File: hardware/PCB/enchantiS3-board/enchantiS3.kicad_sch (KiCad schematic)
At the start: 74 parts, among them J1 USB_C_Receptacle_USB2.0, Q1 BSS138, Q2 BSS138, Q3 BSS138, SW1 B3U-1000P, SW2 B3U-1000P, U1 USBLC6-2P6, U2 MCP73871, U3 NCP167AMX330TBG, U4 NCP167AMX180TBG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

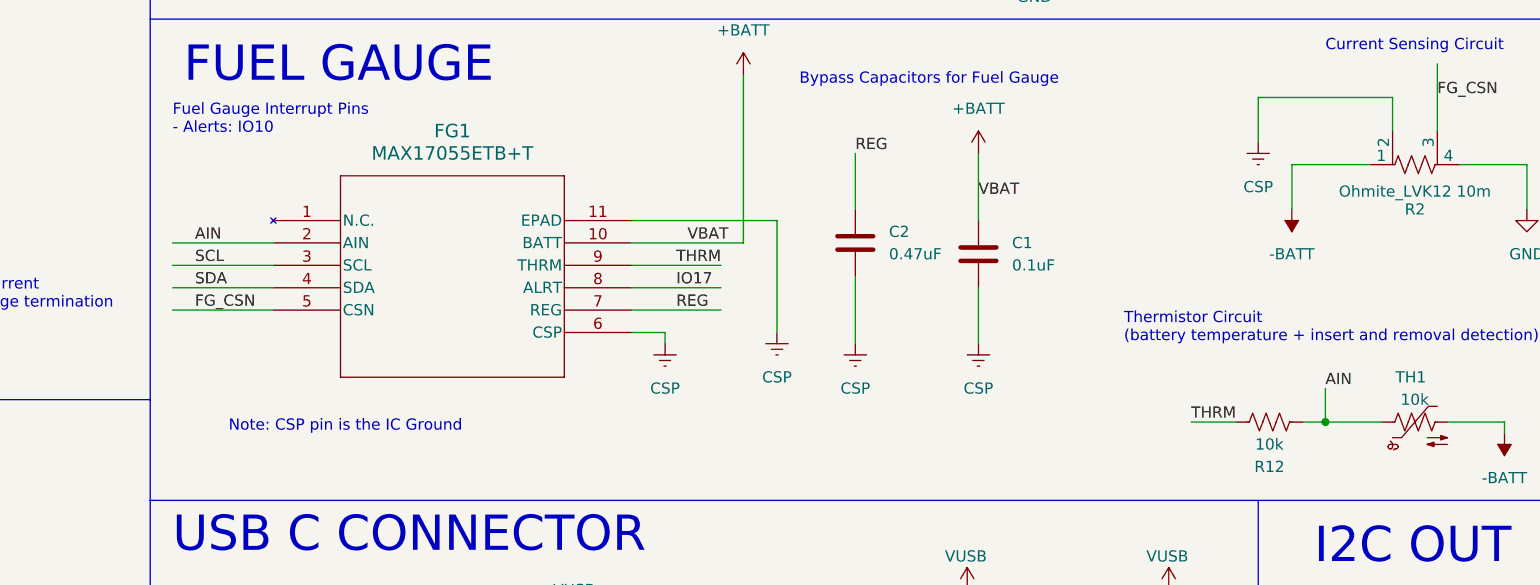
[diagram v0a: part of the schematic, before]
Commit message: update enchanti s3 pcb, cleaned up traces around fuel gauge
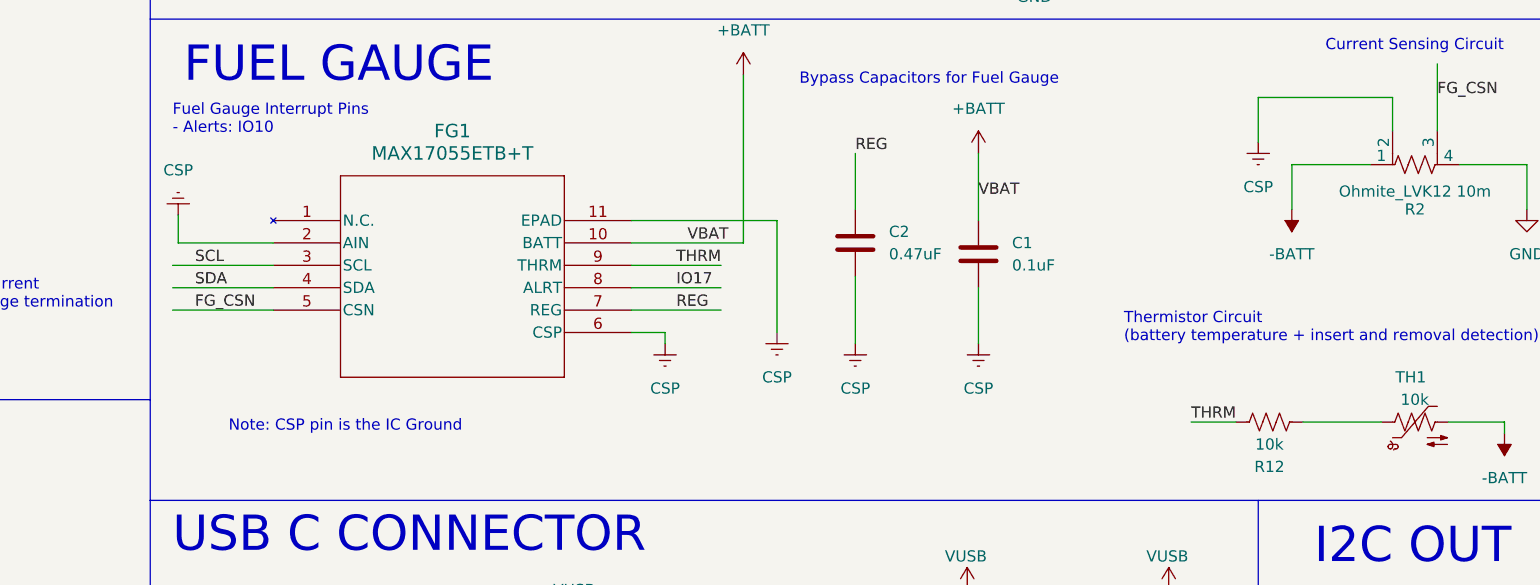
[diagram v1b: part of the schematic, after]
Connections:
- net CSP: now also FG1.2 (AIN)
- net AIN: no longer names the net of R12.1, TH1.1
- net AIN: no longer FG1.2 (AIN)
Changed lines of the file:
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@@
   (junction (at 309.88 33.02) (diameter 0) (color 0 0 0 0)
   )
-  (junction (at 243.84 166.37) (diameter 0) (color 0 0 0 0)
-  )
   (junction (at 363.22 45.72) (diameter 0) (color 0 0 0 0)
   )
@@
     (stroke (width 0) (type default))
   )
-  (wire (pts (xy 241.3 166.37) (xy 243.84 166.37))
-    (stroke (width 0) (type default))
-  )
   (wire (pts (xy 31.75 59.69) (xy 38.1 59.69))
     (stroke (width 0) (type default))
@@
     (stroke (width 0) (type default))
   )
-  (wire (pts (xy 243.84 162.56) (xy 243.84 166.37))
-    (stroke (width 0) (type default))
-  )
   (wire (pts (xy 382.27 96.52) (xy 391.16 96.52))
     (stroke (width 0) (type default))
@@
     (stroke (width 0) (type default))
   )
-  (wire (pts (xy 113.03 146.05) (xy 124.46 146.05))
-    (stroke (width 0) (type default))
-  )
   (polyline (pts (xy 408.94 110.49) (xy 408.94 111.76))
     (stroke (width 0) (type default))
@@
     (stroke (width 0) (type default))
   )
-  (wire (pts (xy 243.84 166.37) (xy 250.19 166.37))
+  (wire (pts (xy 241.3 166.37) (xy 250.19 166.37))
     (stroke (width 0) (type default))
   )
@@
     (stroke (width 0) (type default))
   )
+  (wire (pts (xy 113.665 142.875) (xy 113.665 146.05))
+    (stroke (width 0) (type default))
+  )
   (wire (pts (xy 30.48 44.45) (xy 38.1 44.45))
     (stroke (width 0) (type default))
@@
     (stroke (width 0) (type default))
   )
+  (wire (pts (xy 113.665 146.05) (xy 124.46 146.05))
+    (stroke (width 0) (type default))
+  )
   (wire (pts (xy 379.73 162.56) (xy 387.35 162.56))
     (stroke (width 0) (type default))
@@
     (effects (font (size 1.27 1.27)) (justify left bottom))
   )
-  (label "AIN" (at 115.57 146.05 0) (fields_autoplaced)
-    (effects (font (size 1.27 1.27)) (justify left bottom))
-  )
   (label "COPI" (at 214.63 256.54 180) (fields_autoplaced)
     (effects (font (size 1.27 1.27)) (justify right bottom))
@@
     (effects (font (size 1.27 1.27)) (justify left bottom))
   )
-  (label "AIN" (at 243.84 162.56 0) (fields_autoplaced)
-    (effects (font (size 1.27 1.27)) (justify left bottom))
-  )
   (label "VBAT" (at 171.45 146.05 0) (fields_autoplaced)
     (effects (font (size 1.27 1.27)) (justify left bottom))
@@
         )
       )
+    )
+  )
+  (symbol (lib_id "max17055-symbol:CSP") (at 113.665 141.605 180) (unit 1)
+    (in_bom yes) (on_board yes) (dnp no) (fields_autoplaced)
+    (property "Reference" "#ICGND05" (at 113.665 135.255 0)
+      (effects (font (size 1.27 1.27)) hide)
+    )
+    (property "Value" "CSP" (at 113.665 137.795 0)
+      (effects (font (size 1.27 1.27)))
+    )
+    (property "Footprint" "" (at 117.475 141.605 0)
+      (effects (font (size 1.27 1.27)) hide)
+    )
+    (property "Datasheet" "" (at 117.475 141.605 0)
+      (effects (font (size 1.27 1.27)) hide)
+    )
+    (pin "1")
+    (instances
+      (project "enchantiS3"
+        (path "/1e57a4ff-0c95-4e2b-9e56-d9bf8e99c9a1"
+          (reference "#ICGND05") (unit 1)
+        )
+      )
+      (project "tstick_pcb"
+        (path "/ecdbf224-0069-4dc3-a7df-492909ab59c7"
+          (reference "#ICGND04") (unit 1)
+        )
+      )

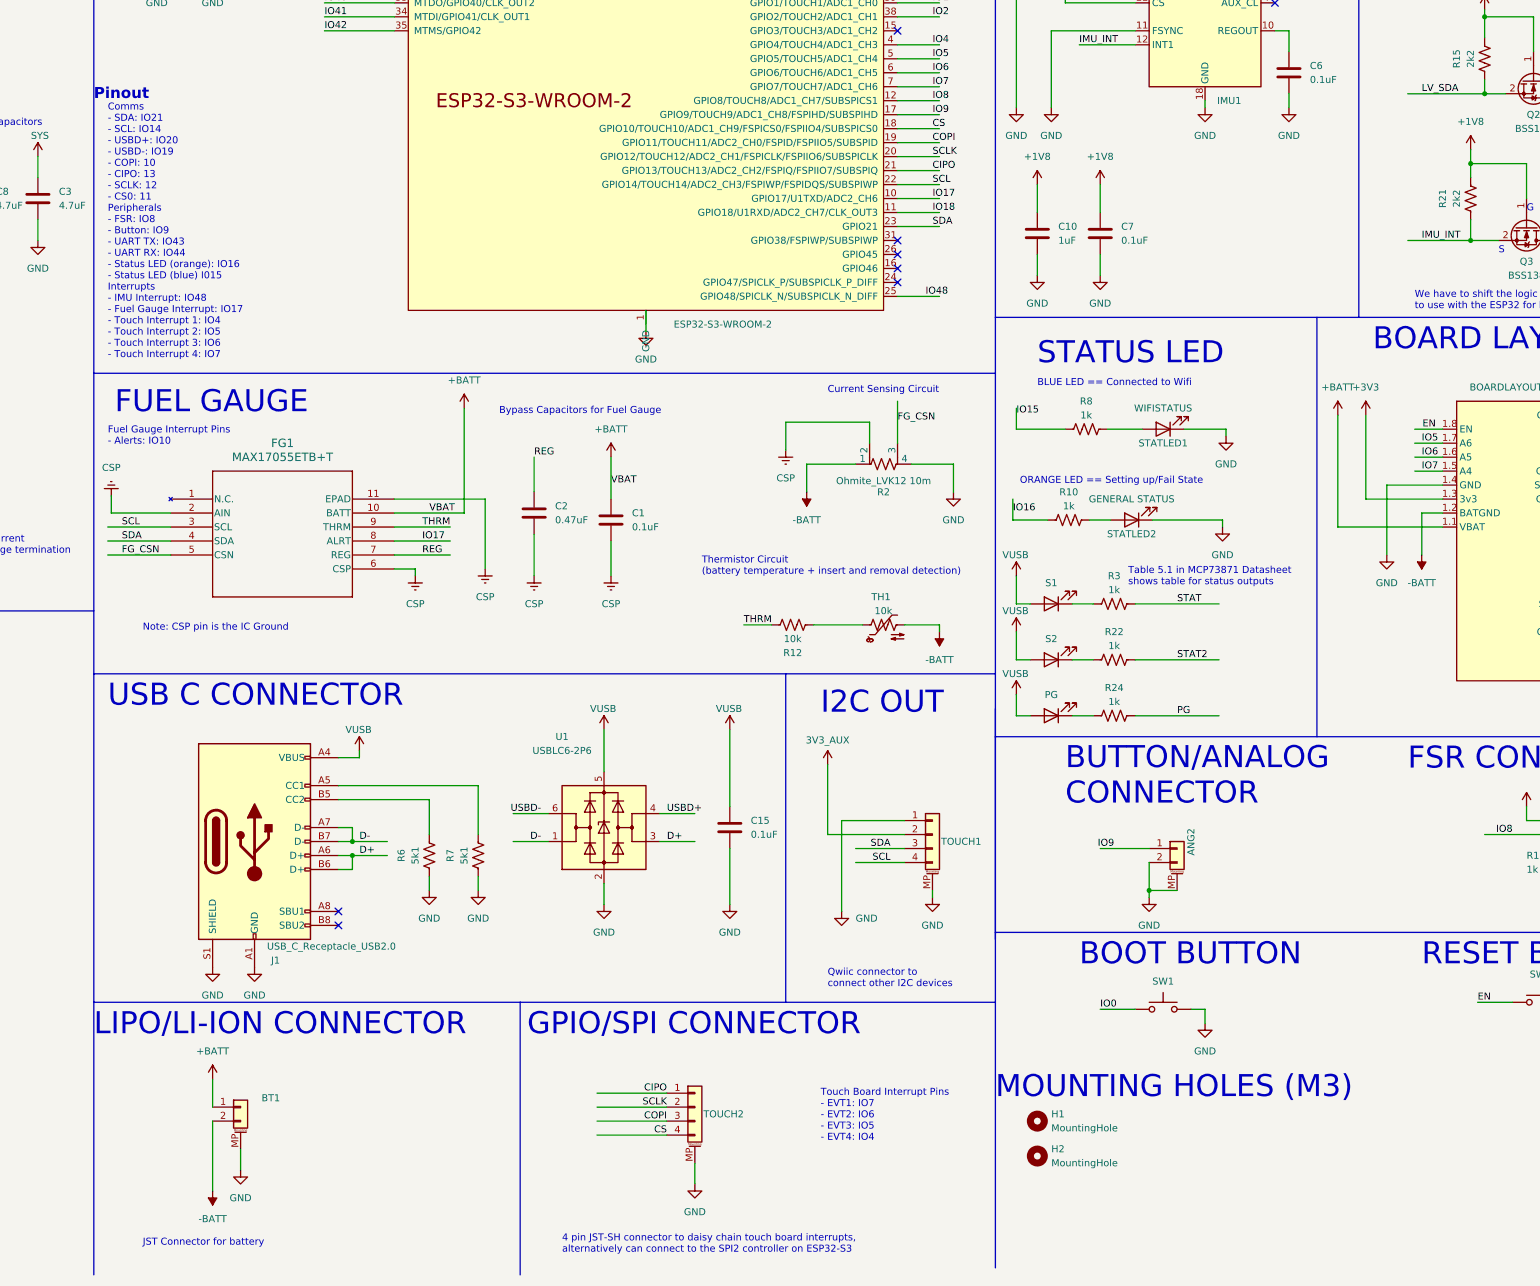
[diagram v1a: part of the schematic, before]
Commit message: changed to MAX17262 fuel gauge, removed unneeded part libraries
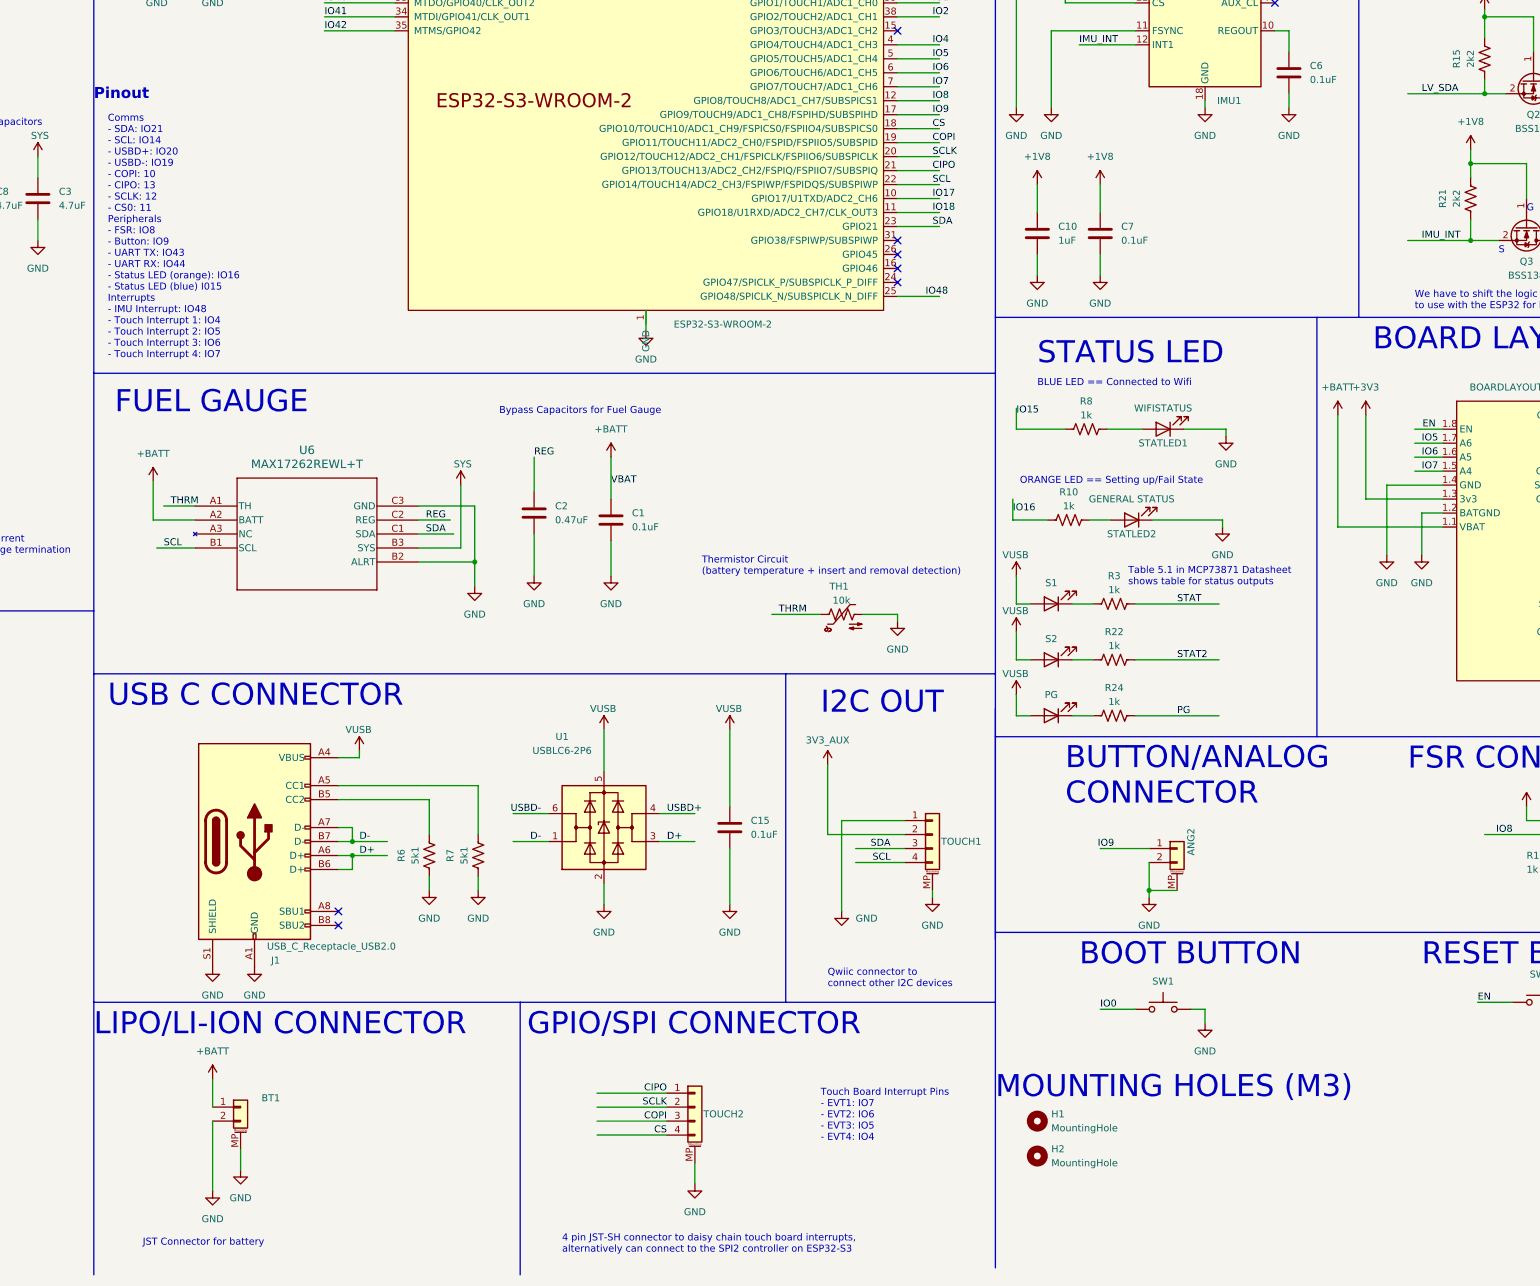
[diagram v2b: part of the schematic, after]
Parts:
- removed FG1: MAX17055ETB+T, max17055-footprints:21-100013A_T102A2&plus_1C_MXM, symbol max17055-symbol:MAX17055ETB+T
- removed R12: 10k, Resistor_SMD:R_0402_1005Metric, symbol Device:R_US
- removed R2: Ohmite_LVK12 10m, ul_LVK12R010CER-footprints:LVK12_OHM-L, symbol Device:R_Shunt_US
- added SYS7: SYS, symbol power-symbols:VSYS
- added U6: MAX17262REWL+T, max17262-footprints:21-100221A_W91G1&plus_3_MXM, symbol max17262:MAX17262REWL+T
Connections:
- net -BATT is gone; now on net GND: BOARDLAYOUT1.1.2 (BATGND), BT1.2 (Pin_2), TH1.2
- net CSP is gone; now on net GND: C1.2, C2.2
- net +BATT: now also U6.A2 (BATT)
- net GND: now also U6.B2 (ALRT), U6.C3 (GND)
- net REG: now also U6.C2 (REG)
- net SCL: now also U6.B1 (SCL)
- net SDA: now also U6.C1 (SDA)
- net SYS: now also SYS7.1 (SYS), U6.B3 (SYS)
- net THRM: now also TH1.1, U6.A1 (TH)
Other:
- note added: "Comms - SDA: IO21 - SCL: IO14 - USBD+: IO20 - USBD-: IO19 - COPI: 10 - CIPO: 13 - SCLK: 12 - CS0: 11 Peripherals - FSR: IO8 - Button: IO9 - UART TX: IO43 - UART RX: IO44 - Status LED (orange): IO16 - Status LED (blue) I015 Interrupts - IMU Interrupt: IO48 - Touch Interrupt 1: IO4 - Touch Interrupt 2: IO5 - Touch Interrupt 3: IO6 - Touch Interrupt 4: IO7"
- note removed: "Comms - SDA: IO21 - SCL: IO14 - USBD+: IO20 - USBD-: IO19 - COPI: 10 - CIPO: 13 - SCLK: 12 - CS0: 11 Peripherals - FSR: IO8 - Button: IO9 - UART TX: IO43 - UART RX: IO44 - Status LED (orange): IO16 - Status LED (blue) I015 Interrupts - IMU Interrupt: IO48 - Fuel Gauge Interrupt: IO17 - Touch Interrupt 1: IO4 - Touch Interrupt 2: IO5 - Touch Interrupt 3: IO6 - Touch Interrupt 4: IO7"
- note removed: "Current Sensing Circuit"
- note removed: "Fuel Gauge Interrupt Pins - Alerts: IO10"
- note removed: "Note: CSP pin is the IC Ground"
- moved on the sheet: TH1
